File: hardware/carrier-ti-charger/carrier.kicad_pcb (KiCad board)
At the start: 4 copper layers, 105 x 95 mm, 143 parts, among them J1 MC-107DMS, J10 J_ADS_MAIN ADSBee J5, J11 J_ADS_GNSS ADSBee J4, J12 CONTROLS, J2 J_NTC 100k ENTC-EB-100K4262-02, J3 J_BAT JST-PH 2mm, J4 J_THERM 60C NC, J5 J_GNSS GPS-18037 J5, J6 J_ESP_A support, J7 J_ESP_B power/UART, J8 J_ESP_C I2C, J9 J_ESP_D support, Q2 AO3401A, Q3 AO3401A, Q4 AO3401A, Q6 2N7002, Q7 AO3401A, Q8 2N7002, Q9 2N7002, SW1 K3-1280S-F1, SW2 K3-1280S-F1, SW3 K3-1280S-F1, U10 BMP581, U11 LM73100RPWR, U12 LM73100RPWR, U13 TCA9534PWR, U4 MAX77757JEFG420+T, U5 TLV840CADL29DBVR 2.9V, U6 TPS61088RHLR, U7 TPS22975DSGR, U8 MAX17048G+T10, U9 SN74LVC1G17DBVR

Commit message: TI charger
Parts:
- removed C34, C7: 2.2u 25V X7R, Capacitor_SMD:C_0603_1608Metric
- removed Q6: 2N7002, Package_TO_SOT_SMD:SOT-23
- removed R37, R6: 6.2k 1%, Resistor_SMD:R_0603_1608Metric
- removed R8: 154k 1%, Resistor_SMD:R_0603_1608Metric
- added C41: 10u 25V X7R, Capacitor_SMD:C_0805_2012Metric, F.Cu at (120.7, 104.9)
- added C42: 10u 25V X7R, Capacitor_SMD:C_0805_2012Metric, F.Cu at (118.6, 104.9)
- added C43: 100n 50V, Capacitor_SMD:C_0603_1608Metric, F.Cu at (116.8, 105.2)
- added C44: 100n 50V, Capacitor_SMD:C_0603_1608Metric, F.Cu at (115.1, 113.5)
- added C45: 47n 50V, Capacitor_SMD:C_0603_1608Metric, F.Cu at (106.8, 120.9)
- added C46: 100n 50V, Capacitor_SMD:C_0603_1608Metric, F.Cu at (112.3, 113.0)
- added C47: 10u 25V X7R, Capacitor_SMD:C_0805_2012Metric, F.Cu at (109.0, 114.9)
- added C48: 4.7u 16V X5R, Capacitor_SMD:C_0603_1608Metric, F.Cu at (112.0, 101.5)
- added C49: 1n 50V, Capacitor_SMD:C_0603_1608Metric, F.Cu at (109.9, 112.3)
- added C50: 100n 50V, Capacitor_SMD:C_0603_1608Metric, F.Cu at (122.7, 106.7)
- added C51: 22u 10V X7R, Capacitor_SMD:C_0805_2012Metric, F.Cu at (103.9, 59.9)
- added C52: 22u 10V X7R, Capacitor_SMD:C_0805_2012Metric, F.Cu at (105.9, 59.9)
- added C53: 100n 50V, Capacitor_SMD:C_0603_1608Metric, F.Cu at (143.6, 111.1)
- added Q10: 2N7002, Package_TO_SOT_SMD:SOT-23, F.Cu at (102.1, 126.5)
- added Q11: 2N7002, Package_TO_SOT_SMD:SOT-23, F.Cu at (89.9, 120.1)
- added Q12: 2N7002, Package_TO_SOT_SMD:SOT-23, F.Cu at (128.5, 103.8)
- added R56: 4.7k 1%, Resistor_SMD:R_0603_1608Metric, F.Cu at (105.8, 106.9)
- added R57: 47k 1%, Resistor_SMD:R_0603_1608Metric, F.Cu at (108.9, 103.0)
- added R58: 100k 1%, Resistor_SMD:R_0603_1608Metric, F.Cu at (108.9, 104.5)
- added R59: 80.6k 1%, Resistor_SMD:R_0603_1608Metric, F.Cu at (112.0, 104.5)
- added R60: 768k 1%, Resistor_SMD:R_0603_1608Metric, F.Cu at (104.6, 115.1)
- added R61: 150R, Resistor_SMD:R_0603_1608Metric, F.Cu at (106.6, 109.2)
- added R62: 100k 1%, Resistor_SMD:R_0603_1608Metric, F.Cu at (105.0, 109.2)
- added R63: 47k 1%, Resistor_SMD:R_0603_1608Metric, F.Cu at (127.6, 121.7)
- added R64: 100k 1%, Resistor_SMD:R_0603_1608Metric, F.Cu at (126.9, 124.0)
- added R65: 5.1k 1%, Resistor_SMD:R_0603_1608Metric, F.Cu at (135.5, 119.1)
- added R66: 5.1k 1%, Resistor_SMD:R_0603_1608Metric, F.Cu at (139.8, 119.1)
- added R67: 1M, Resistor_SMD:R_0603_1608Metric, F.Cu at (123.4, 109.0)
- added R68: 1M, Resistor_SMD:R_0603_1608Metric, F.Cu at (127.4, 109.0)
- added R69: 100k 1%, Resistor_SMD:R_0603_1608Metric, F.Cu at (93.5, 121.1)
- added REF**: OSHW-Logo_7.5x8mm_SilkScreen, Symbol:OSHW-Logo_7.5x8mm_SilkScreen, F.Cu at (71.6, 126.5)
- added TP8: CHG_INT_N, carrier:TestPoint_Pad_D1.5mm, F.Cu at (102.2, 109.6)
- added U14: LM73100RPWR, carrier:VQFN-10_L2.0-W2.0-P0.45-HR_LM73100, F.Cu at (125.0, 106.7)
- C12, C16, C27, C28, C29, C30, C31, C37, C38, C39, C40: value 100n -> 100n 50V
- C15: value 2.2u 25V X7R -> 4.7u 16V X5R
- C17: value 47n -> 47n 50V
- C5: value 2.2u 25V X7R -> 100n 50V
- C8: value 100n -> 47n 50V
- L1: value 1uH FXL0630-1R0-M -> 2.2uH FXL0630-2R2-M
- R12, R13, R27, R36, R41, R48, R49, R50, R51, R52, R53, R54, R55: value 100k -> 100k 1%
- R23, R31: value 560R -> 470R
- R33: value 47k -> 47k 1%
- U4: value MAX77757JEFG420+T -> BQ25798RQMR; footprint carrier:FC2QFN-24_L3.0-W3.0-P0.40_MAX77757 -> Package_DFN_QFN:Texas_RQM0029A_VQFN-29_4x4mm_P0.4mm
- moved TP3 57.0 mm to (153.5, 112.0)
- moved U5 32.9 mm to (135.5, 99.3)
- moved R13 32.2 mm to (135.1, 102.7)
- moved C14 28.6 mm to (137.9, 116.8), turned to 0 degrees
- moved R12 25.1 mm to (105.8, 104.5), turned to 0 degrees
- moved C12 24.0 mm to (132.1, 102.7), turned to 180 degrees
- moved C5 22.0 mm to (128.4, 124.0), turned to -90 degrees
- moved C11 13.1 mm to (98.6, 121.3), turned to -90 degrees
- moved C35 10.8 mm to (112.0, 103.0), turned to 0 degrees
- moved C8 8.42 mm to (120.7, 119.4)
- moved C33 6.35 mm to (124.2, 111.0), turned to 0 degrees
- moved TP5 5.84 mm to (129.3, 119.4)
- moved L1 5.31 mm to (114.0, 119.6), turned to 180 degrees
- moved C10 4.40 mm to (117.6, 115.1)
- moved C9 3.22 mm to (112.5, 114.9)
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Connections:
- C33 pad 1: CHG_BYP -> CHG_PMID
- C6 pad 1: CHG_BYP -> CHG_PMID
- C8 pad 1: CHG_BTST -> CHG_BTST1
- C8 pad 2: CHG_SW -> CHG_SW1
- J12 pad 6: CTRL_P7 -> unconnected-(J12-Pin_6-Pad6)
- L1 pad 1: CHG_SW -> CHG_SW1
- L1 pad 2: VSYS -> CHG_SW2
- Q4 pad 1: CHG_INOK_N -> USB_OK_N
- R36 pad 2: CHG_INOK_N -> USB_OK_N
- R55 pad 2: CTRL_P7 -> SW_ON_N
- U13 pad 12: CTRL_P7 -> SW_ON_N
- U4 pad 1: CHG_BTST -> CHG_STAT_N
- U4 pad 10: CHG_VDD -> GND
- U4 pad 11: BAT_TS -> GND
- U4 pad 12: CHG_IFAST -> unconnected-(U4-~{QON}-Pad12)
- U4 pad 13: VBAT -> CHG_DIS
- U4 pad 14: VBAT -> I2C_SCL
- U4 pad 15: VSYS -> I2C_SDA
- U4 pad 16: VSYS -> BAT_TS
- U4 pad 17: CHG_PVL -> CHG_ILIM
- U4 pad 18: GND -> CHG_BATP
- U4 pad 19: GND -> CHG_BTST2
- U4 pad 2: CHG_INOK_N -> USB_VBUS
- U4 pad 20: CHG_SW -> CHG_PROG
- U4 pad 21: CHG_SW -> CHG_INT_N
- U4 pad 22: CHG_BYP -> VBAT
- U4 pad 23: USB_VBUS -> VBAT
- U4 pad 24: USB_VBUS -> CHG_SDRV
- U4 pad 3: CHG_STAT_N -> USB_VBUS
- U4 pad 4: USB_CC2 -> CHG_BTST1
- U4 pad 5: USB_CC1 -> CHG_REGN
- U4 pad 8: GND -> USB_VBUS
- U4 pad 9: GND -> USB_VBUS
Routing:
- net RAIL_5V: track 220.2 -> 146.2 mm
- net ESP_5V_D: track 4.79 -> 65.5 mm, vias 0 -> 2
- net PWR_EN: track 85.4 -> 44.6 mm
- net USB_CC2: track 45.7 -> 8.84 mm
- net CHG_INOK_N: track 34.2 -> 0.00 mm, vias 2 -> 0
- net USB_G2: track 0.00 -> 32.6 mm, vias 0 -> 2
- net USB_CC1: track 40.6 -> 9.18 mm
- net VBAT: track 63.7 -> 34.6 mm, vias 5 -> 2
- net CHG_DIS: track 23.6 -> 50.2 mm, vias 2 -> 3
- net CHG_REGN: track 0.00 -> 24.0 mm, vias 0 -> 4
- net CTRL_P7: track 21.8 -> 0.00 mm, vias 1 -> 0
- net SW_ON_N: track 0.00 -> 21.2 mm, vias 0 -> 2
- net VSYS: track 71.4 -> 91.7 mm, vias 29 -> 11
- net CHG_BTST2: track 0.00 -> 19.6 mm, vias 0 -> 2
- net I2C_SDA: track 54.0 -> 70.3 mm
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- added copper zone on F.Cu, net CHG_SW1
- added copper zone on In2.Cu, net CHG_SW1
- added copper zone on F.Cu, net CHG_SW2
- added copper zone on In2.Cu, net CHG_SW2
- added copper zone on F.Cu, net USB_VBUS_J1
- removed copper zone on F.Cu, net CHG_SW
- removed copper zone on In2.Cu, net CHG_SW
- removed copper zone on In2.Cu, net VSYS
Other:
- board text added: "Bottom plate sits on the solder mask through a thermal pad (no mask opening: vias of several nets lie under it). Outline on Dwgs.User."

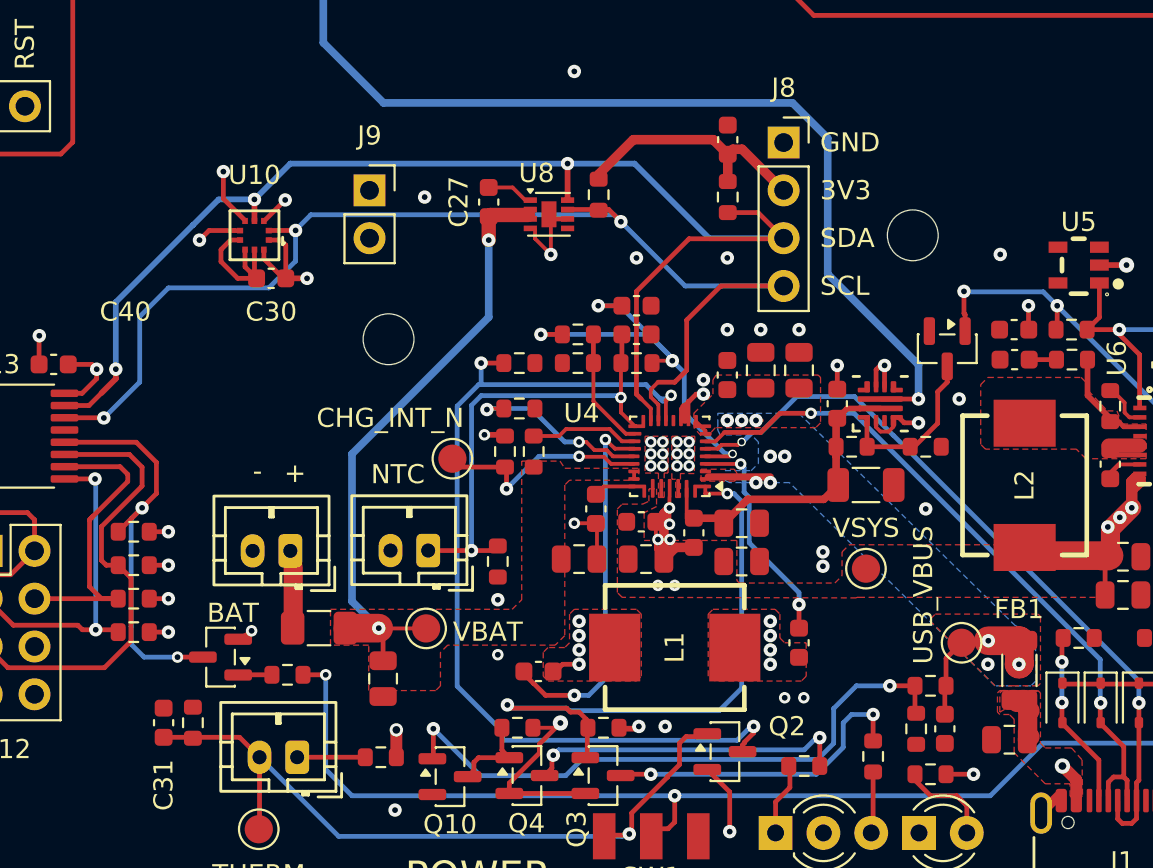
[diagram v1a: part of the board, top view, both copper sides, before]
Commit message: Align I2C resistors for 100kHZ ops.
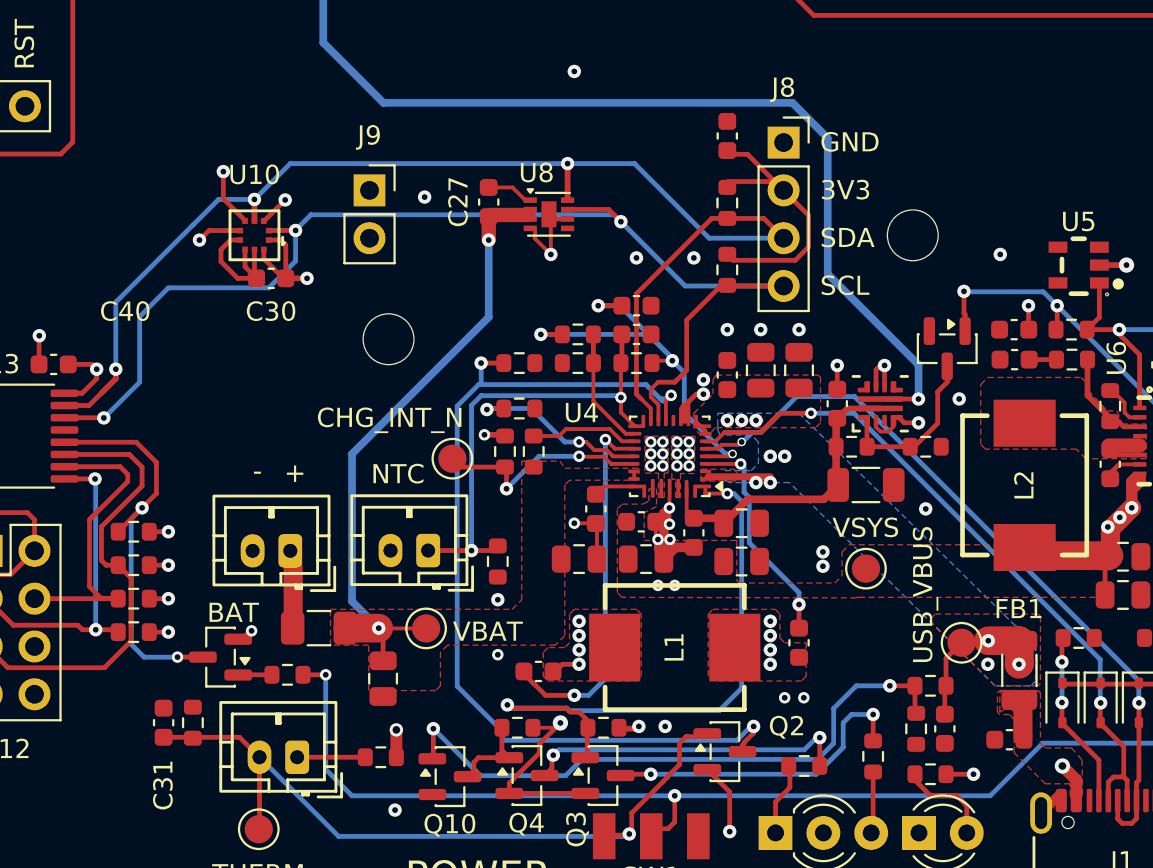
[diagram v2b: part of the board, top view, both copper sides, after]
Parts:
- C1: value 4.7u 50V X7R -> 4.7u 16V X5R; footprint Capacitor_SMD:C_0805_2012Metric -> Capacitor_SMD:C_0603_1608Metric
- R19, R20: value 4.7k -> 2.2k
- moved R20 7.92 mm to (116.8, 99.6)
- moved R19 0.31 mm to (116.8, 96.0)
- moved C29 0.20 mm to (116.8, 92.5)
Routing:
- net I2C_SDA: track 70.3 -> 67.7 mm
- net USB_VBUS_J1: track 17.3 -> 16.3 mm
- net ESP_3V3: track 209.2 -> 210.2 mm
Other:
- board text removed: "BAT"
- board text removed: "NTC"
- board text removed: "THERM"

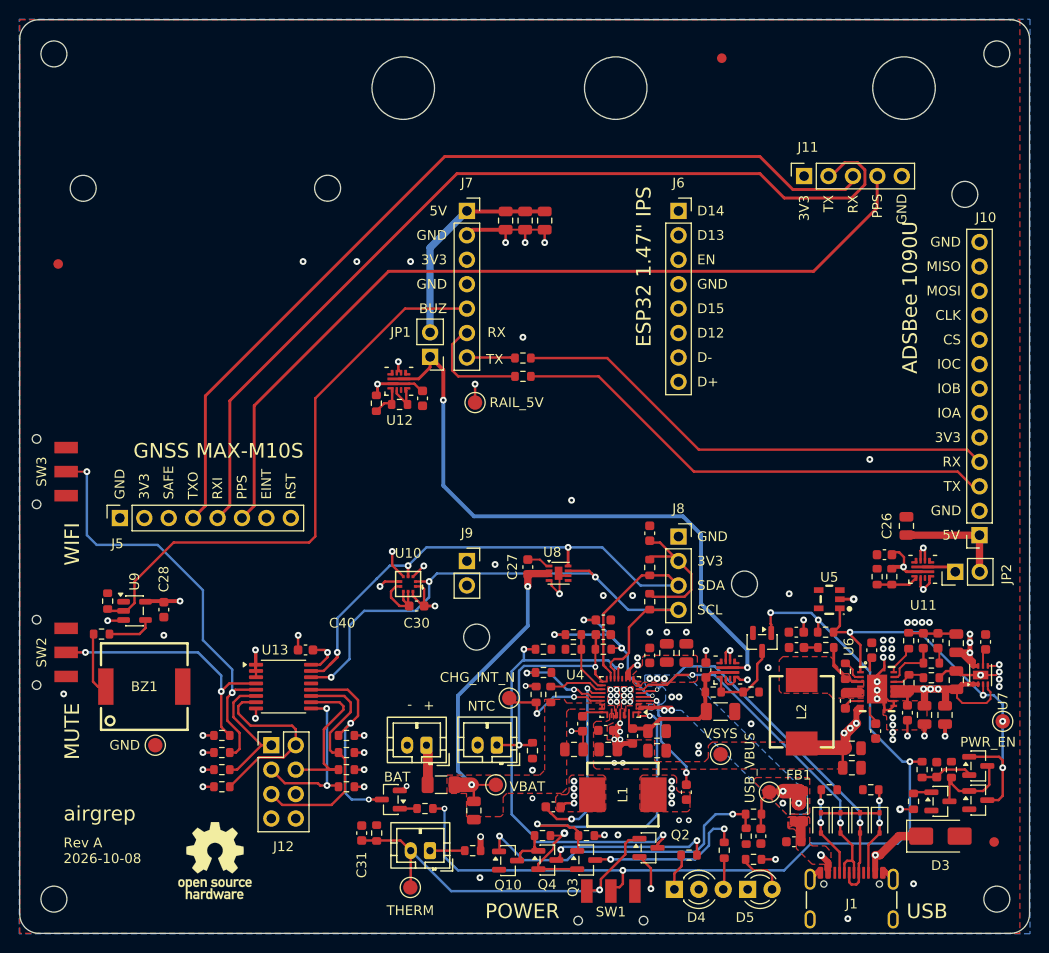
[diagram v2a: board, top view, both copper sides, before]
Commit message: Switch parts (BMP580, TPS259474L) due to stock shortage.
Also, add overvoltage (OVLO) protection.
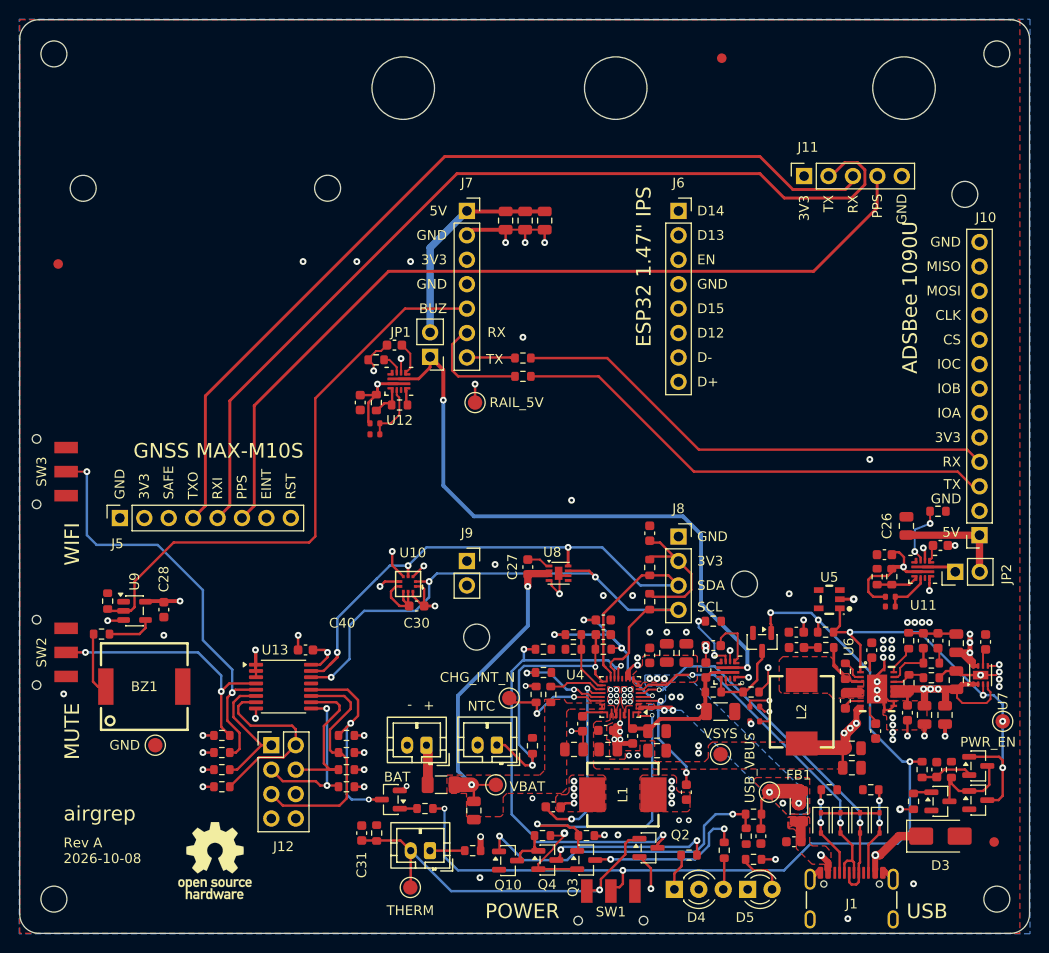
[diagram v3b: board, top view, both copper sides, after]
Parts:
- added C54: 2.2n 50V, Capacitor_SMD:C_0603_1608Metric, F.Cu at (90.3, 72.9)
- added C55: 2.2n 50V, Capacitor_SMD:C_0603_1608Metric, F.Cu at (123.4, 104.1)
- added C56: 2.2n 50V, Capacitor_SMD:C_0603_1608Metric, F.Cu at (147.1, 93.7)
- added R70: 1.65k, Resistor_SMD:R_0603_1608Metric, F.Cu at (146.8, 90.2)
- added R71: 1.65k, Resistor_SMD:R_0603_1608Metric, F.Cu at (88.4, 74.4)
- added R72: 1.65k, Resistor_SMD:R_0603_1608Metric, F.Cu at (123.4, 101.6)
- added R73: 5.1k, carrier:R_0402_1005Metric_NoSilk, F.Cu at (141.9, 99.1)
- added R74: 1.5k, carrier:R_0402_1005Metric_NoSilk, F.Cu at (141.9, 100.1)
- added R75: 5.1k, carrier:R_0402_1005Metric_NoSilk, F.Cu at (88.3, 81.0)
- added R76: 1.5k, carrier:R_0402_1005Metric_NoSilk, F.Cu at (88.3, 82.2)
- added R77: 5.1k, carrier:R_0402_1005Metric_NoSilk, F.Cu at (127.8, 110.5)
- added R78: 1.5k, carrier:R_0402_1005Metric_NoSilk, F.Cu at (127.8, 112.0)
- U10: value BMP581 -> BMP580
- U11, U12, U14: value LM73100RPWR -> TPS259474LRPWR
- moved C38 6.49 mm to (86.7, 78.9)
- moved R60 0.51 mm to (104.6, 114.6), turned to 90 degrees
- moved R44 0.07 mm to (88.4, 78.9)
- moved R45 0.06 mm to (90.8, 79.1)
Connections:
- U11 pad 2: GND -> U11_OVLO
- U11 pad 7: unconnected-(U11-DVDT-Pad7) -> U11_DVDT
- U11 pad 9: GND -> U11_ILM
- U12 pad 2: GND -> U12_OVLO
- U12 pad 7: unconnected-(U12-DVDT-Pad7) -> U12_DVDT
- U12 pad 9: GND -> U12_ILM
- U14 pad 2: GND -> U14_OVLO
- U14 pad 7: unconnected-(U14-DVDT-Pad7) -> U14_DVDT
- U14 pad 9: GND -> U14_ILM
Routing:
- net CHG_PMID: track 16.3 -> 27.3 mm, vias 0 -> 2
- net RAIL_5V: track 146.2 -> 156.2 mm
- net U14_OVLO: track 0.00 -> 9.73 mm, vias 0 -> 2
- net U14_ILM: track 0.00 -> 6.73 mm, vias 0 -> 2
- net U11_ILM: track 0.00 -> 6.48 mm, vias 0 -> 2
- net U12_OVLO: track 0.00 -> 6.23 mm
- net U14_DVDT: track 0.00 -> 5.79 mm
- net U11_OVLO: track 0.00 -> 4.80 mm
- net BAT_TS: track 25.4 -> 29.7 mm
- net GND: track 109.2 -> 112.8 mm, vias 76 -> 78
- net U12_DVDT: track 0.00 -> 3.43 mm
- net U12_ILM: track 0.00 -> 2.20 mm
- net U11_DVDT: track 0.00 -> 1.70 mm
- net USB_VBUS: track 29.4 -> 27.9 mm
- net CTRL_P5: track 16.7 -> 16.0 mm
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
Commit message: Add reset FET switch.
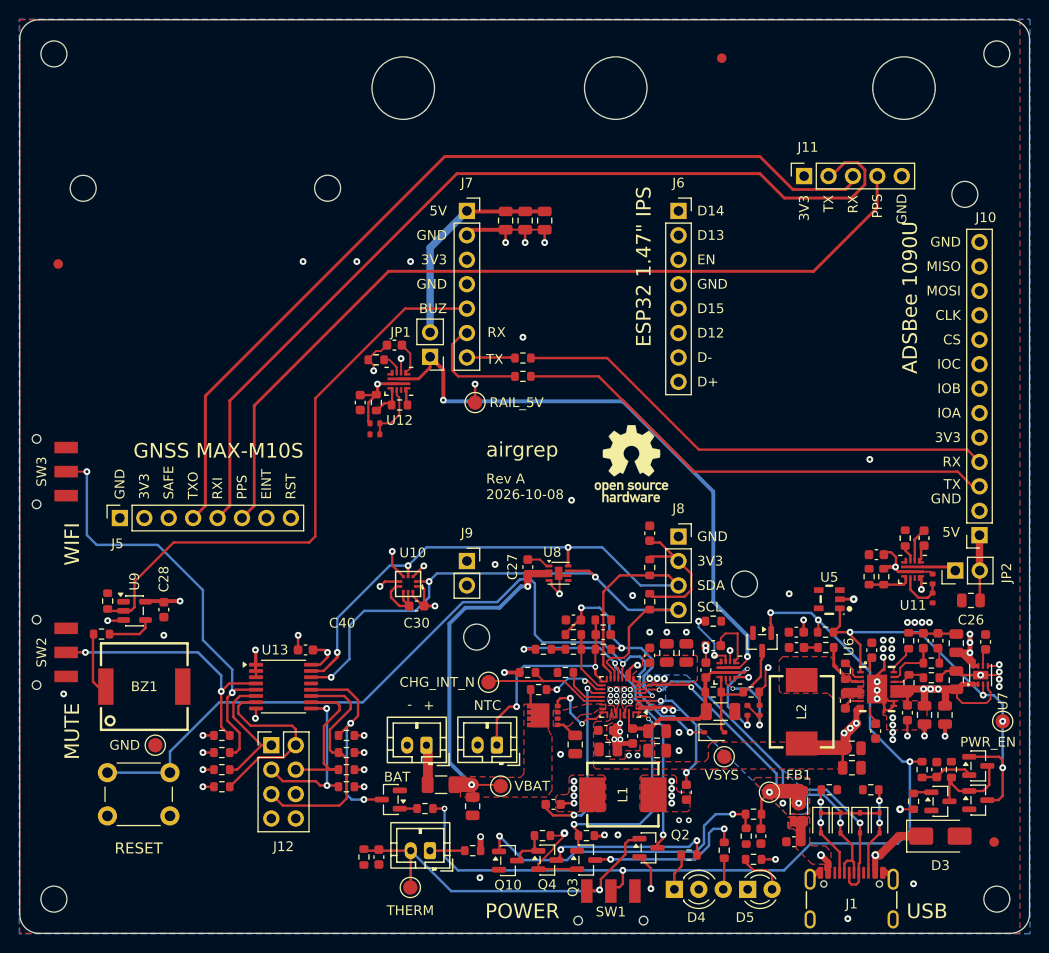
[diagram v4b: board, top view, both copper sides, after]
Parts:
- removed C49: 1n 50V, Capacitor_SMD:C_0603_1608Metric
- added D10: BAT54WS, Diode_SMD:D_SOD-323, F.Cu at (123.6, 113.2)
- added Q13: CSD17575Q3, carrier:VSON-8_3.3x3.3mm_CSD17575Q3, F.Cu at (105.8, 111.4)
- added SW4: RESET 6x6, Button_Switch_THT:SW_PUSH_6mm, F.Cu at (60.5, 117.3)
- C47: value 10u 25V X7R -> 22u 10V X7R
- moved REF** 59.8 mm to (114.9, 85.2)
- moved R60 15.0 mm to (112.0, 101.5), turned to 0 degrees
- moved C26 10.2 mm to (150.2, 99.4), turned to 180 degrees
- moved R73 4.77 mm to (146.3, 97.2), turned to -90 degrees
- moved R74 4.48 mm to (146.3, 99.2), turned to -90 degrees
- moved R70 4.40 mm to (143.4, 93.0), turned to 90 degrees
- moved C48 3.11 mm to (108.9, 101.5), turned to 180 degrees
- moved C31 3.07 mm to (88.7, 126.1), turned to -90 degrees
- moved R10 2.83 mm to (87.1, 126.1), turned to -90 degrees
- moved TP8 2.72 mm to (100.1, 108.0)
- moved R62 2.45 mm to (104.1, 106.9), turned to 0 degrees
- moved R56 2.29 mm to (108.1, 106.9), turned to 180 degrees
- moved C56 1.86 mm to (145.4, 93.0), turned to 90 degrees
- moved R61 1.37 mm to (105.3, 108.7), turned to 180 degrees
- moved R78 1.25 mm to (128.3, 110.9), turned to 90 degrees
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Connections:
- C47 pad 1: VBAT -> CHG_BAT
- U4 pad 12: unconnected-(U4-~{QON}-Pad12) -> CHG_QON_N
- U4 pad 22: VBAT -> CHG_BAT
- U4 pad 23: VBAT -> CHG_BAT
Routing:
- net CHG_QON_N: track 0.00 -> 86.5 mm, vias 0 -> 2
- net CHG_DIS: track 50.2 -> 34.6 mm
- net CHG_STAT_N: track 31.3 -> 22.6 mm
- net CHG_SDRV: track 2.23 -> 7.79 mm, vias 0 -> 2
- net BAT_TS: track 29.7 -> 24.6 mm
- net CHG_PROG: track 9.81 -> 5.03 mm, vias 2 -> 0
- net U11_ILM: track 6.48 -> 1.74 mm, vias 2 -> 0
- net ADS_5V: track 11.4 -> 6.78 mm
- net VBAT: track 34.6 -> 39.2 mm
- net /Charger BQ25798/ESP_PMID_EN: track 8.66 -> 13.0 mm
- net RAIL_5V: track 156.2 -> 152.0 mm
- net CHG_INT_N: track 11.2 -> 14.2 mm, vias 2 -> 0
- net CHG_REGN: track 24.0 -> 21.2 mm, vias 4 -> 3
- net ESP_5V_D: track 65.5 -> 62.9 mm
- net CHG_BAT: track 0.00 -> 2.15 mm
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- added copper zone on F.Cu, net CHG_BAT
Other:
- board text added: "RESET"
